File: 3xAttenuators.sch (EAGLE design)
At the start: 9 parts

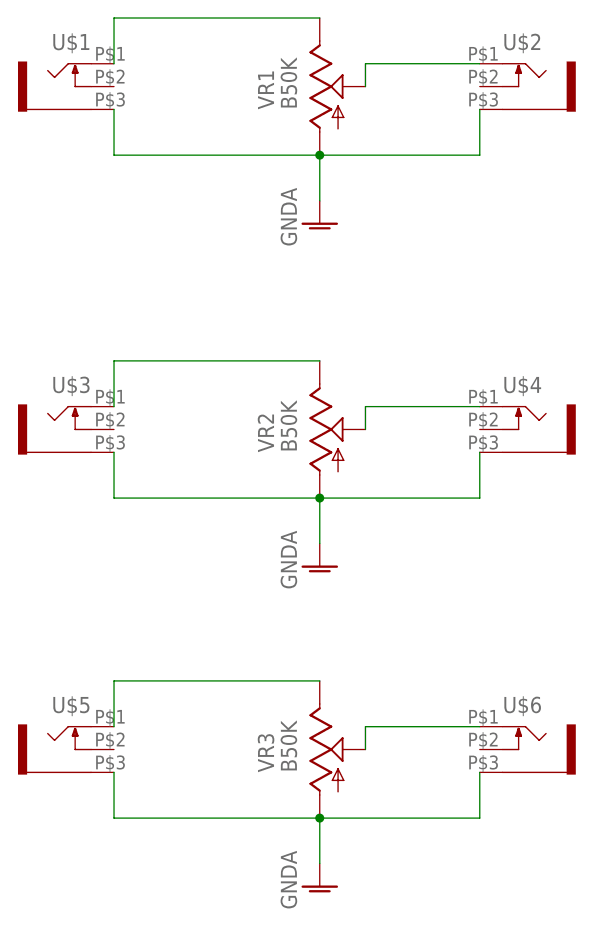
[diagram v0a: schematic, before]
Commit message: adding rendered images of pcbs
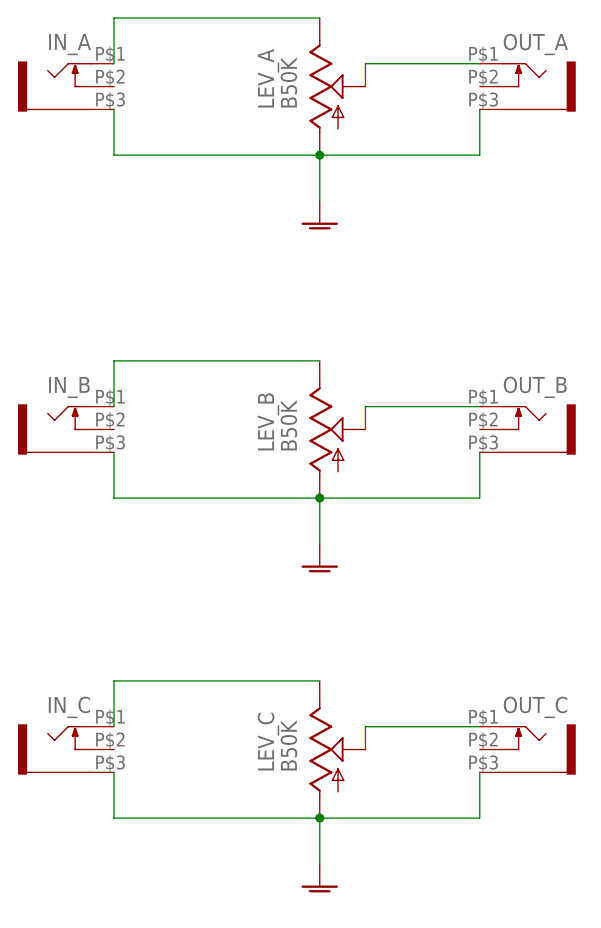
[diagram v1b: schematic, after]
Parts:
- renumbered U$1 to IN_A, U$2 to OUT_A, U$3 to IN_B, U$4 to OUT_B, U$5 to IN_C, U$6 to OUT_C, VR1 to LEV_A, VR2 to LEV_B, VR3 to LEV_C
